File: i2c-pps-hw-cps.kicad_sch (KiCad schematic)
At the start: 36 parts, among them Q1 SiR880BDP, Q2 SiR880BDP, Q3 SiR880BDP, Q4 SiR880BDP, U1 BQ25758S

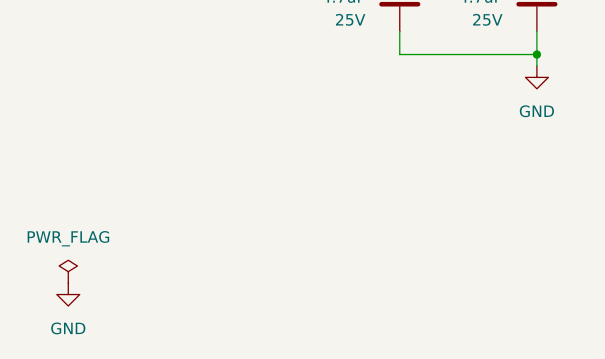
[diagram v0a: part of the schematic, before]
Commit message: Fix errors and warnings reported by ERC
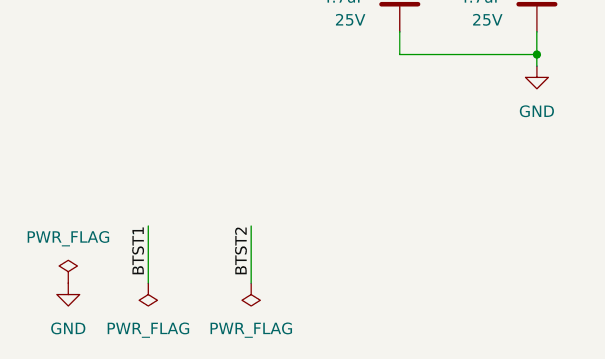
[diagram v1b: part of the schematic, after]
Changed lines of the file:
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@@
 	(wire
 		(pts
+			(xy 38.1 190.5) (xy 38.1 196.85)
+		)
+		(stroke
+			(width 0)
+			(type default)
+		)
+	)
+	(wire
+		(pts
 			(xy 148.59 54.61) (xy 157.48 54.61)
 		)
@@
 	(wire
 		(pts
+			(xy 26.67 190.5) (xy 26.67 196.85)
+		)
+		(stroke
+			(width 0)
+			(type default)
+		)
+	)
+	(wire
+		(pts
 			(xy 63.5 95.25) (xy 63.5 101.6)
 		)
@@
 		)
 	)
+	(label "BTST1"
+		(at 26.67 190.5 270)
+		(effects
+			(font
+				(size 1.27 1.27)
+			)
+			(justify right bottom)
+		)
+	)
 	(label "ACP"
 		(at 199.39 107.95 0)
@@
 		)
 	)
+	(label "BTST2"
+		(at 38.1 190.5 270)
+		(effects
+			(font
+				(size 1.27 1.27)
+			)
+			(justify right bottom)
+		)
+	)
 	(label "VOUT_Filtered"
 		(at 171.45 139.7 180)
@@
 			)
 		)
-		(property "Description" "70.6A Id, 80V Vds N-Channel MOSFET, 6.2mOhm Ron, 19.5nC Qg(typ), PowerPAK-8"
+		(property "Description" "70.6A Id, 80V Vds N-Channel MOSFET, 5.3mOhm Ron, 19.5 nC Qg(typ), PowerPAK-8"
 			(at 119.38 41.91 0)
 			(effects
@@
 			)
 		)
-		(property "Description" "70.6A Id, 80V Vds N-Channel MOSFET, 6.2mOhm Ron, 19.5nC Qg(typ), PowerPAK-8"
+		(property "Description" "70.6A Id, 80V Vds N-Channel MOSFET, 5.3mOhm Ron, 19.5 nC Qg(typ), PowerPAK-8"
 			(at 160.02 67.31 0)
 			(effects
@@
 	)
 	(symbol
-		(lib_name "SiR880BDP_1")
 		(lib_id "i2c-pps-hw:SiR880BDP")
 		(at 119.38 67.31 0)
@@
 			)
 		)
-		(property "Description" "70.6A Id, 80V Vds N-Channel MOSFET, 6.2mOhm Ron, 19.5nC Qg(typ), PowerPAK-8"
+		(property "Description" "70.6A Id, 80V Vds N-Channel MOSFET, 5.3mOhm Ron, 19.5 nC Qg(typ), PowerPAK-8"
 			(at 119.38 67.31 0)
 			(effects
@@
 	)
 	(symbol
+		(lib_id "power:PWR_FLAG")
+		(at 26.67 196.85 180)
+		(unit 1)
+		(exclude_from_sim no)
+		(in_bom yes)
+		(on_board yes)
+		(dnp no)
+		(fields_autoplaced yes)
+		(property "Reference" "#FLG03"
+			(at 26.67 198.755 0)
+			(effects
+				(font
+					(size 1.27 1.27)
+				)
+				(hide yes)
+			)
+		)
+		(property "Value" "PWR_FLAG"
+			(at 26.67 201.93 0)
+			(effects
+				(font
+					(size 1.27 1.27)
+				)
+			)
+		)
+		(property "Footprint" ""
+			(at 26.67 196.85 0)
+			(effects
+				(font
+					(size 1.27 1.27)
+				)
+				(hide yes)
+			)
+		)
+		(property "Datasheet" "~"
+			(at 26.67 196.85 0)
+			(effects
+				(font
+					(size 1.27 1.27)
+				)
+				(hide yes)
+			)
+		)
+		(property "Description" "Special symbol for telling ERC where power comes from"
+			(at 26.67 196.85 0)
+			(effects
+				(font
+					(size 1.27 1.27)
+				)
+				(hide yes)
+			)
+		)
+		(pin "1"
+		)
+		(instances
+			(project "i2c-pps-hw"
+				(path "/512c4d3f-92f6-4670-bf9b-2123d46bbde3/7e783548-a00d-43c3-b9e7-95f97450619e"
+					(reference "#FLG03")
+					(unit 1)
+				)
+			)
+		)
+	)
+	(symbol
 		(lib_id "Device:C")
 		(at 215.9 158.75 270)
@@
 			)
 		)
-		(property "Description" "70.6A Id, 80V Vds N-Channel MOSFET, 6.2mOhm Ron, 19.5nC Qg(typ), PowerPAK-8"
+		(property "Description" "70.6A Id, 80V Vds N-Channel MOSFET, 5.3mOhm Ron, 19.5 nC Qg(typ), PowerPAK-8"
 			(at 160.02 41.91 0)
 			(effects
@@
 					(unit 1)
 				)
+			)
+		)
+	)
+	(symbol
+		(lib_id "power:PWR_FLAG")
+		(at 38.1 196.85 180)
+		(unit 1)
+		(exclude_from_sim no)
+		(in_bom yes)
+		(on_board yes)
+		(dnp no)
+		(fields_autoplaced yes)
+		(property "Reference" "#FLG04"
+			(at 38.1 198.755 0)
+			(effects
+				(font
+					(size 1.27 1.27)
+				)
+				(hide yes)
+			)
+		)
+		(property "Value" "PWR_FLAG"
+			(at 38.1 201.93 0)
+			(effects
+				(font
+					(size 1.27 1.27)
+				)
+			)
+		)
+		(property "Footprint" ""
+			(at 38.1 196.85 0)
+			(effects
+				(font
+					(size 1.27 1.27)
+				)
+				(hide yes)
+			)
+		)
+		(property "Datasheet" "~"
+			(at 38.1 196.85 0)
+			(effects
+				(font
+					(size 1.27 1.27)
+				)
+				(hide yes)
+			)
+		)
+		(property "Description" "Special symbol for telling ERC where power comes from"
+			(at 38.1 196.85 0)
+			(effects
+				(font
+					(size 1.27 1.27)
+				)
+				(hide yes)
+			)
+		)
+		(pin "1"
+		)
+		(instances
+			(project "i2c-pps-hw"
+				(path "/512c4d3f-92f6-4670-bf9b-2123d46bbde3/7e783548-a00d-43c3-b9e7-95f97450619e"
+					(reference "#FLG04")
+					(unit 1)
+				)

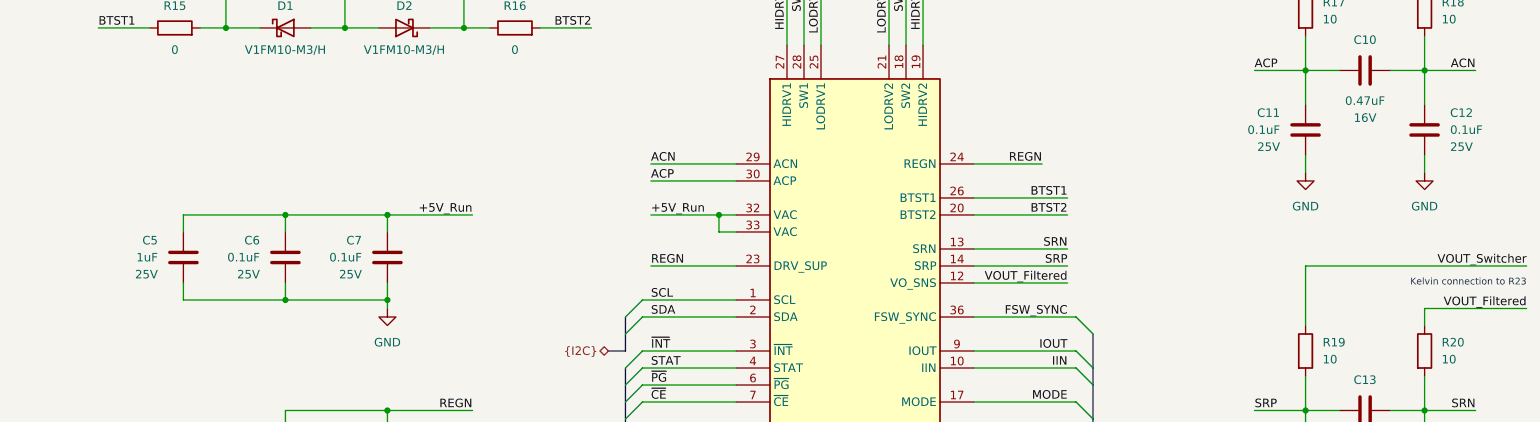
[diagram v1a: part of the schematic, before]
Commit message: Select market available components
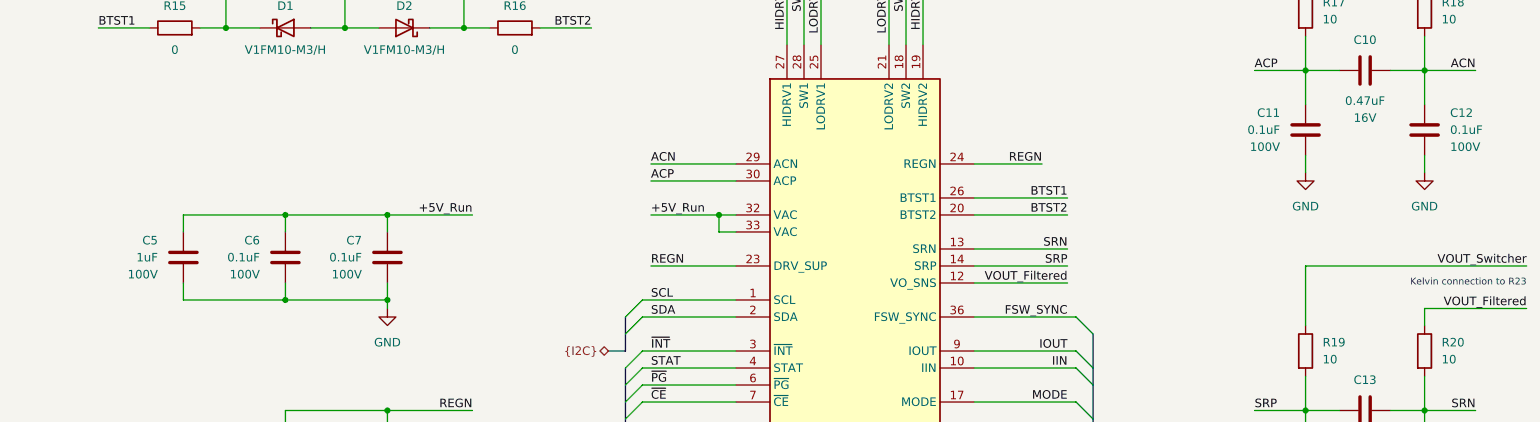
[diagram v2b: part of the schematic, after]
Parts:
- C10, C13: Manufacturer (none) -> Samsung Electro-Mechanics; Part Number (none) -> CL10B474KO8NNNC
- C11, C12, C6, C7: Manufacturer (none) -> Taiyo Yuden; Part Number (none) -> HMK107B7104KAHT; Rated Voltage 25V -> 100V
- C14, C15: Manufacturer (none) -> Taiyo Yuden; Part Number (none) -> HMK107B7104KAHT
- C3, C4: Manufacturer (none) -> KEMET; Part Number (none) -> C0603C104K3RACTU
- C5: Manufacturer (none) -> KYOCERA AVX; Part Number (none) -> 08051C105K4Z2A; Rated Voltage 25V -> 100V
- C8, C9: Manufacturer (none) -> TDK Corporation; Part Number (none) -> CGA4J1X7R1E475K125AE
- D1, D2: Manufacturer (none) -> Vishay General Semiconductor - Diodes Division; Part Number (none) -> V1FM10-M3/H
- L1: footprint (none) -> i2c-pps-hw:L_Bourns_SRP1038A_10.0x11.0mm; Manufacturer (none) -> Bourns Inc; Part Number (none) -> SRP1038A-100M
- Q1, Q2, Q3, Q4: Part Number (none) -> SIR880BDP-T1-RE3
- R10, R11, R12, R13, R15, R16: Manufacturer (none) -> YAGEO; Part Number (none) -> RC0603JR-070RL
- R14: Manufacturer (none) -> Vishay Dale; Part Number (none) -> CRCW08050000Z0EAC
- R17, R18, R19, R20: Manufacturer (none) -> YAGEO; Part Number (none) -> RC0603FR-0710RL
- U1: Part Number (none) -> BQ25758SRRVR

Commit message: Add thermal vias to the power stage transistors
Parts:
- Q1, Q2, Q3, Q4: footprint Package_SO:PowerPAK_SO-8_Single -> i2c-pps-hw:PowerPAK_SO-8_Single_ThermalVias
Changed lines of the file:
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@@
 			)
 		)
-		(property "Footprint" "Package_SO:PowerPAK_SO-8_Single"
+		(property "Footprint" "i2c-pps-hw:PowerPAK_SO-8_Single_ThermalVias"
 			(at 124.46 43.815 0)
 			(effects
@@
 			)
 		)
-		(property "Footprint" "Package_SO:PowerPAK_SO-8_Single"
+		(property "Footprint" "i2c-pps-hw:PowerPAK_SO-8_Single_ThermalVias"
 			(at 154.94 69.215 0)
 			(effects
@@
 			)
 		)
-		(property "Footprint" "Package_SO:PowerPAK_SO-8_Single"
+		(property "Footprint" "i2c-pps-hw:PowerPAK_SO-8_Single_ThermalVias"
 			(at 124.46 69.215 0)
 			(effects
@@
 			)
 		)
-		(property "Footprint" "Package_SO:PowerPAK_SO-8_Single"
+		(property "Footprint" "i2c-pps-hw:PowerPAK_SO-8_Single_ThermalVias"
 			(at 154.94 43.815 0)
 			(effects
